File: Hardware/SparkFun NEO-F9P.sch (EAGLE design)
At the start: 61 parts, among them J1 ANTENNA-SMA-GROUNDEDEDGE_SMA, J2 Qwiic Right Angle, J4 Qwiic Right Angle, U1 U-BLOX_NEO-F9P-15B, U2 3.3V

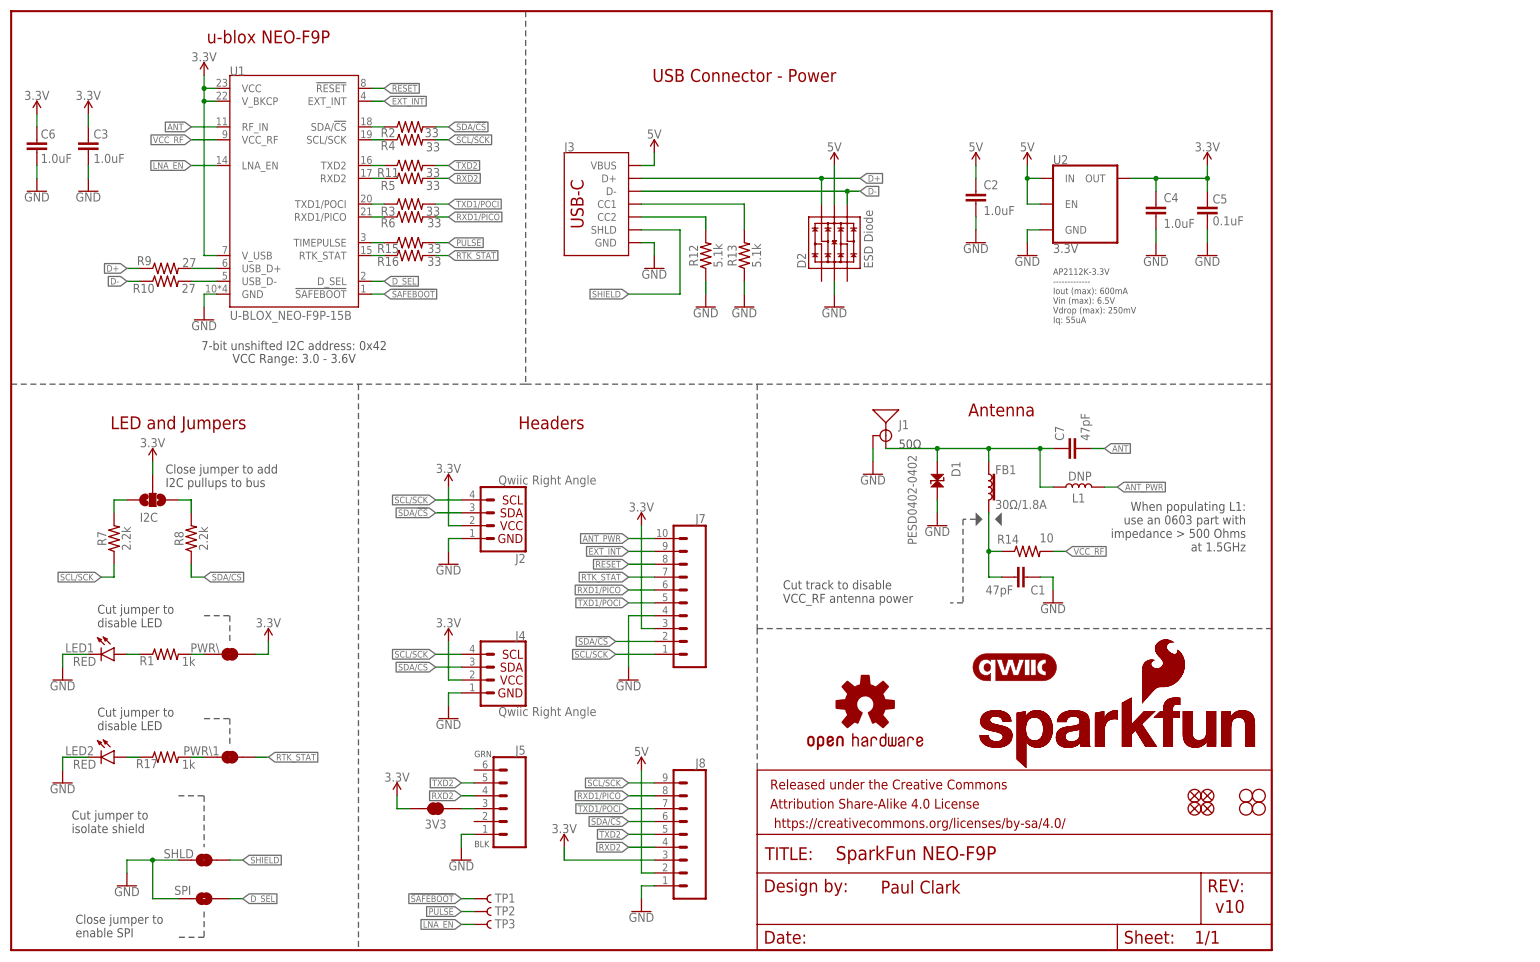
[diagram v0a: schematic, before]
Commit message: Add backup batt. Add PPS LED and PTH. Change silk. Fix RTK LED.
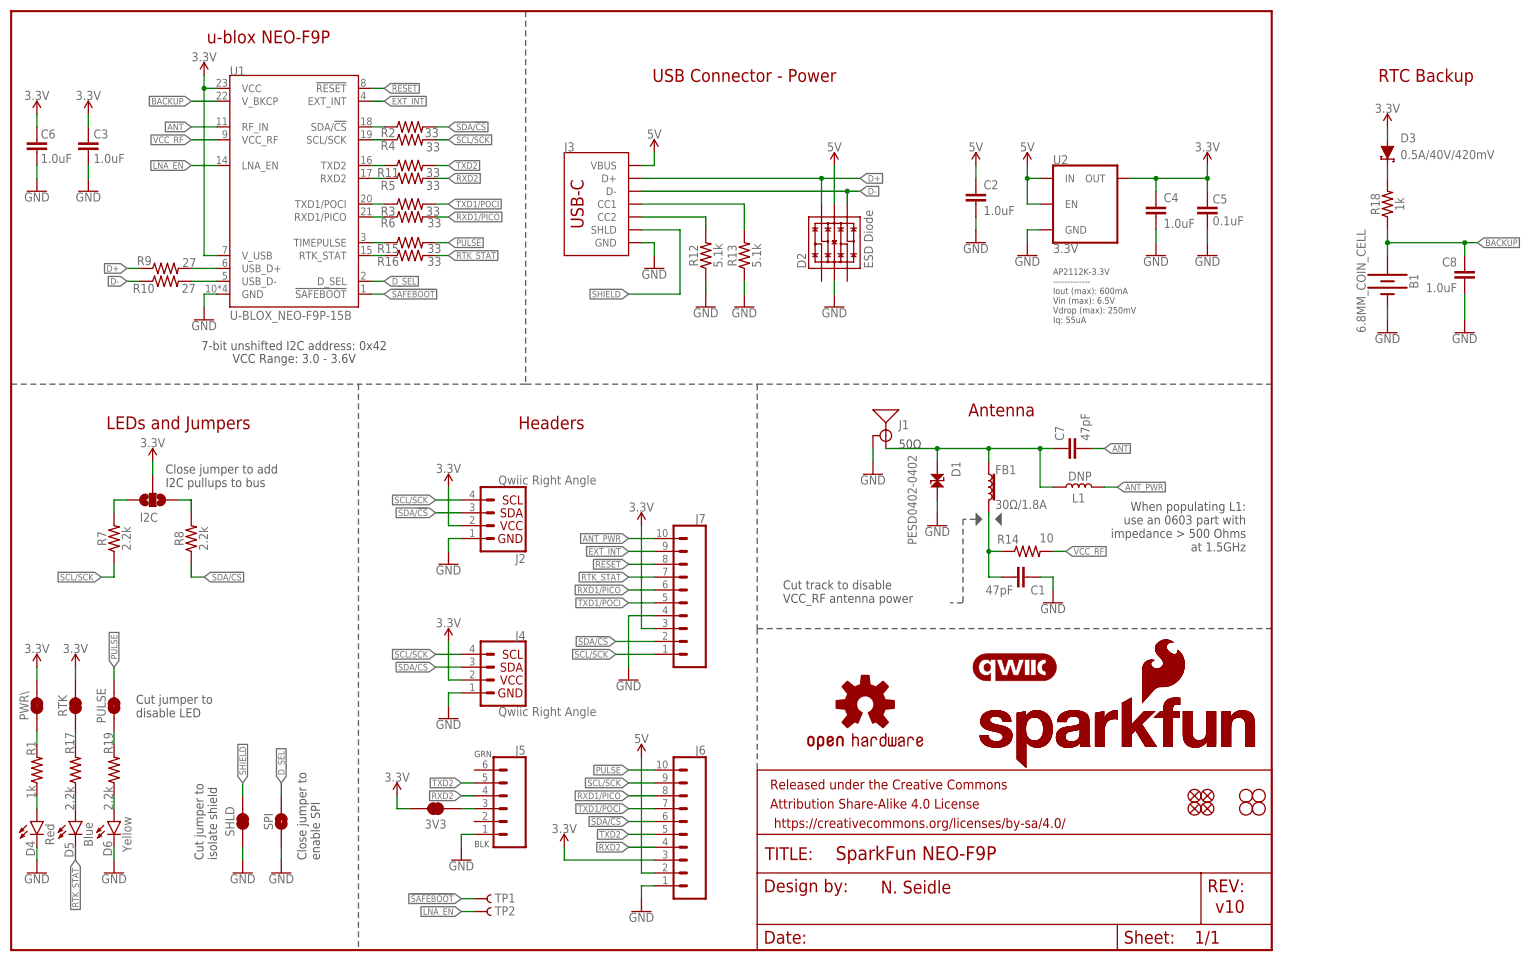
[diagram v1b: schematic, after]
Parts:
- removed J8: (no value), SparkFun-Connectors:CONN_09NO_SILK
- removed LED1, LED2: RED, SparkFun-LED:LED-RED0603
- removed PWR\1: JUMPER-SMT_2_NC_TRACE_SILK, SparkFun-Jumpers:JUMPER-SMT_2_NC_TRACE_SILK
- removed TP3: TEST-POINTPOGO_PTH, SparkFun-Connectors:TEST-POINTPOGO_PTH
- added B1: 6.8MM_COIN_CELL, SparkFun-Batteries:ML414H_IV01E_BATTERY
- added C8: 1.0uF, SparkFun-Capacitors:1.0UF-0603-16V-10%-X7R
- added D3: 0.5A/40V/420mV, SparkFun-DiscreteSemi:DIODE-SCHOTTKY-PMEG4005EJ
- added D4: Red, SparkFun-LED:LED-RED0603
- added D5: Blue, SparkFun-LED:LED-BLUE0603
- added D6: Yellow, SparkFun-LED:LED-YELLOW0603
- added J6: (no value), SparkFun-Connectors:CONN_10NO_SILK_PTH_FEMALE
- added PULSE, RTK: JUMPER-SMT_2_NC_TRACE_SILK, SparkFun-Jumpers:JUMPER-SMT_2_NC_TRACE_SILK
- added R18: 1k, SparkFun-Resistors:1KOHM-0603-1/10W-1%
- added R19: 2.2k, SparkFun-Resistors:2.2KOHM-0603-1/10W-1%
- LOGO3: value SFE_LOGO_NAME_FLAME.1_INCH -> SFE_LOGO_NAME_FLAME7_MM; device SparkFun-Aesthetics:SFE_LOGO_NAME_FLAME.1_INCH -> SparkFun-Aesthetics:SFE_LOGO_NAME_FLAME7_MM
- R17: value 1k -> 2.2k; device SparkFun-Resistors:1KOHM-0603-1/10W-1% -> SparkFun-Resistors:2.2KOHM-0603-1/10W-1%
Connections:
- new net BACKUP: B1.+, C8.1, R18.1, U1.V_BKCP
- new net N$20: D3.C, R18.2
- new net N$21: D6.A, R19.1
- new net N$22: PULSE.1, R19.2
- net 3.3V: now also D3.A, J6.3, RTK.2; no longer J8.3, U1.V_BKCP
- net 5V: now also J6.2; no longer J8.2
- net GND: now also B1.-, C8.2, D4.C, D6.C, J6.1; no longer J8.1, LED1.C, LED2.C
- net LNA_EN: now also TP2.1; no longer TP3.1
- net N$10: now also D4.A; no longer LED1.A
- net N$18: now also D5.A; no longer LED2.A
- net N$19: now also RTK.1; no longer PWR\1.1
- net PULSE: now also J6.10, PULSE.2; no longer TP2.1
- net RTK_STAT: now also D5.C; no longer PWR\1.2
- net RXD1/PICO: now also J6.8; no longer J8.8
- net RXD2: now also J6.4; no longer J8.4
- net SCL/SCK: now also J6.9; no longer J8.9
- net SDA/!CS!: now also J6.6; no longer J8.6
- net TXD1/POCI: now also J6.7; no longer J8.7
- net TXD2: now also J6.5; no longer J8.5
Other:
- note added: "LEDs and Jumpers"
- note added: "N. Seidle"
- note added: "RTC Backup"
- note removed: "LED and Jumpers"
- note removed: "Paul Clark"
- moved on the sheet: PWR\, R1, R17, SHLD, SPI

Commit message: Move R2.
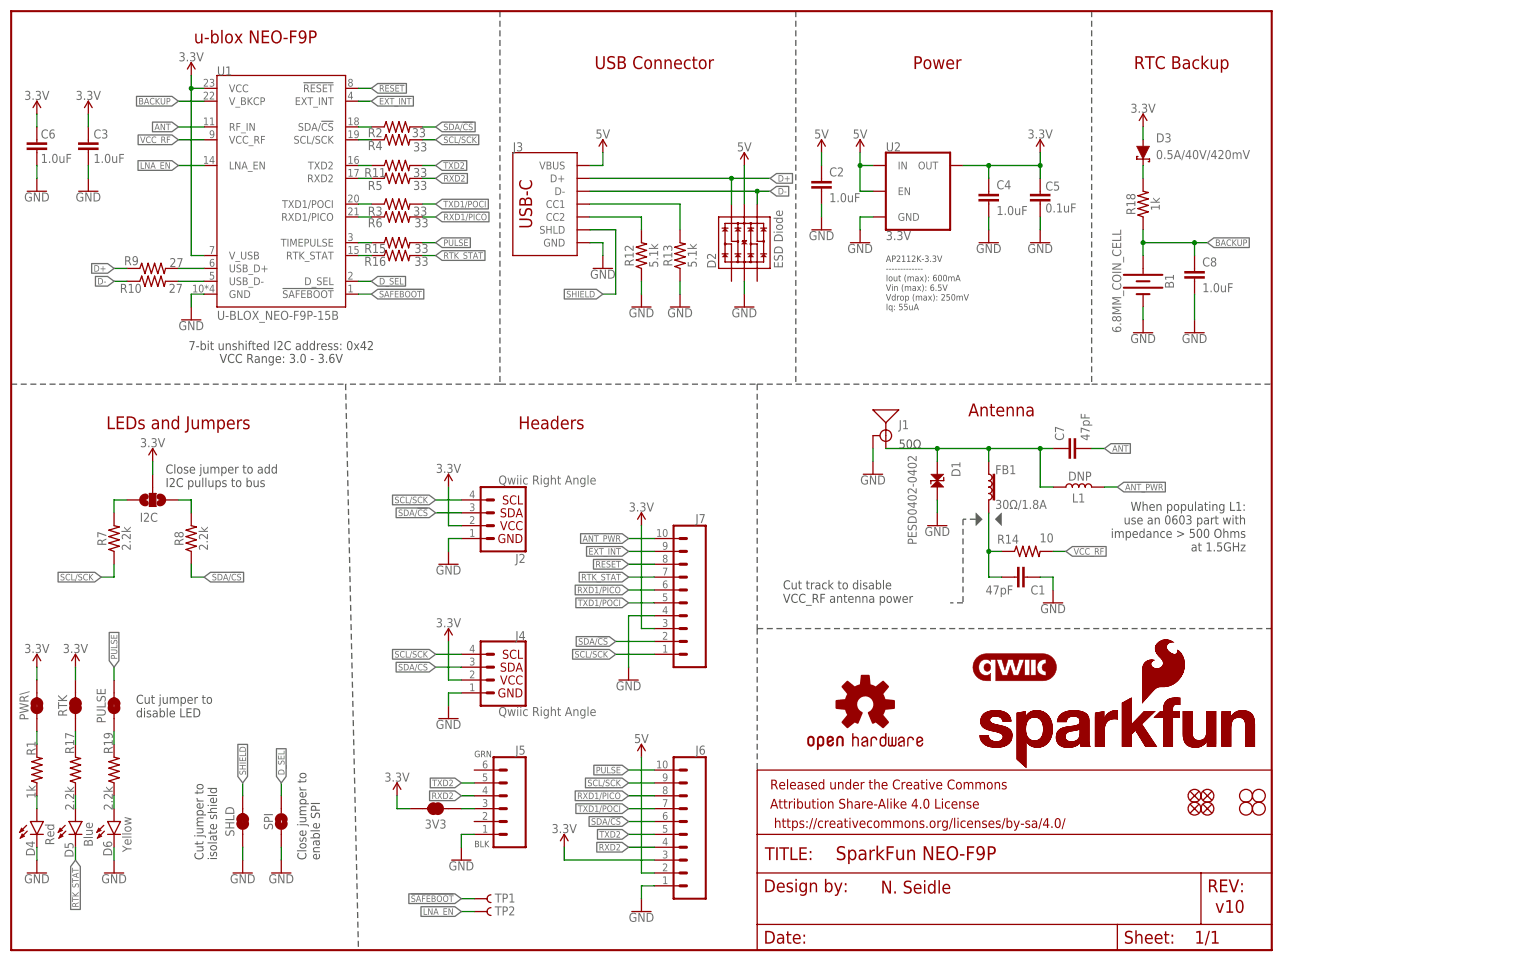
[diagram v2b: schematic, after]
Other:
- note added: "Power"
- note added: "USB Connector"
- note removed: "USB Connector - Power"
- moved on the sheet: B1, C2, C4, C5, C8, D2, D3, J3, R10, R11, R12, R13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
